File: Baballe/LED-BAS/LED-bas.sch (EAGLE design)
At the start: 15 parts, among them Q1 200mA/50V, Q2 200mA/50V, Q3 200mA/50V

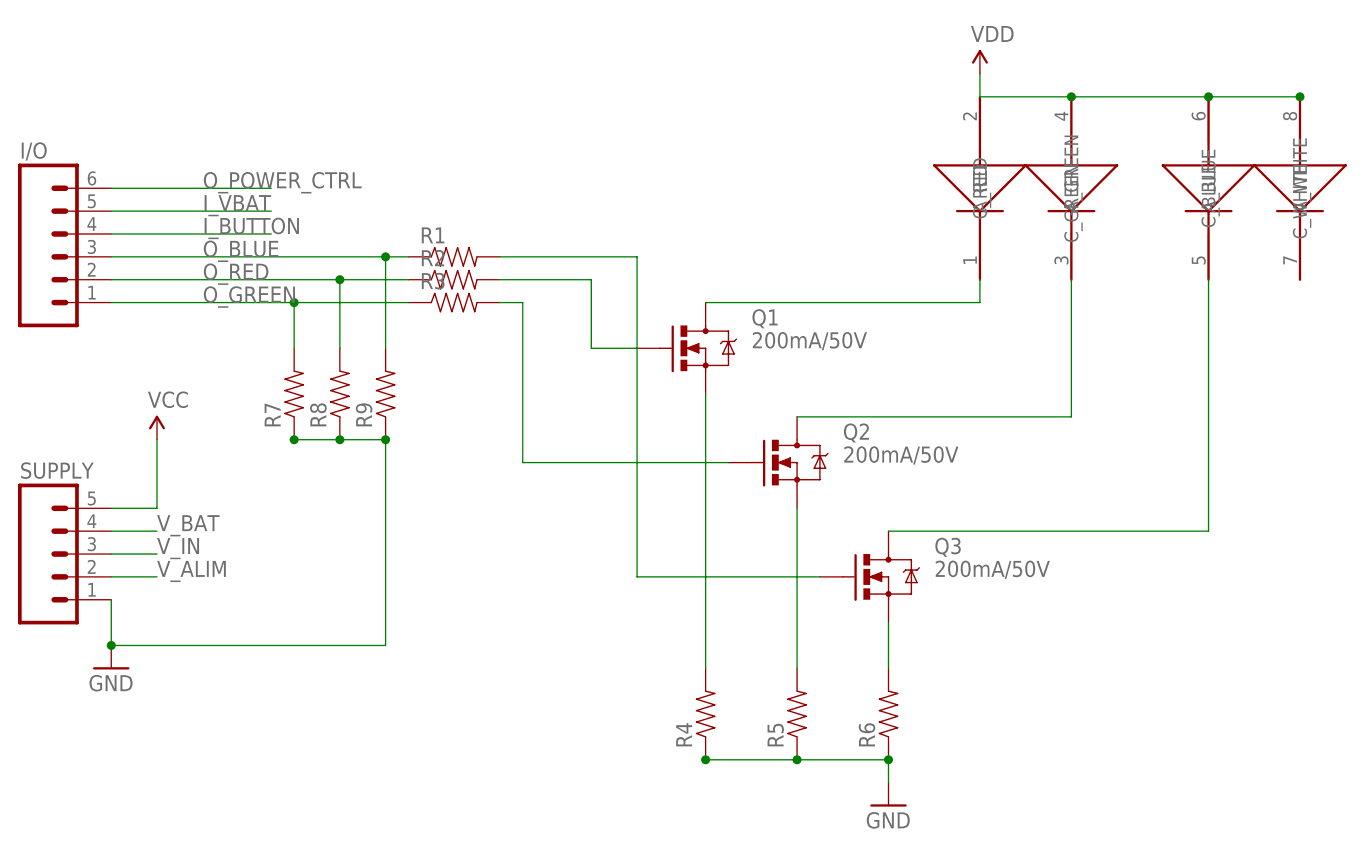
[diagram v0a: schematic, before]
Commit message: Modification sur les modules led et alimentation
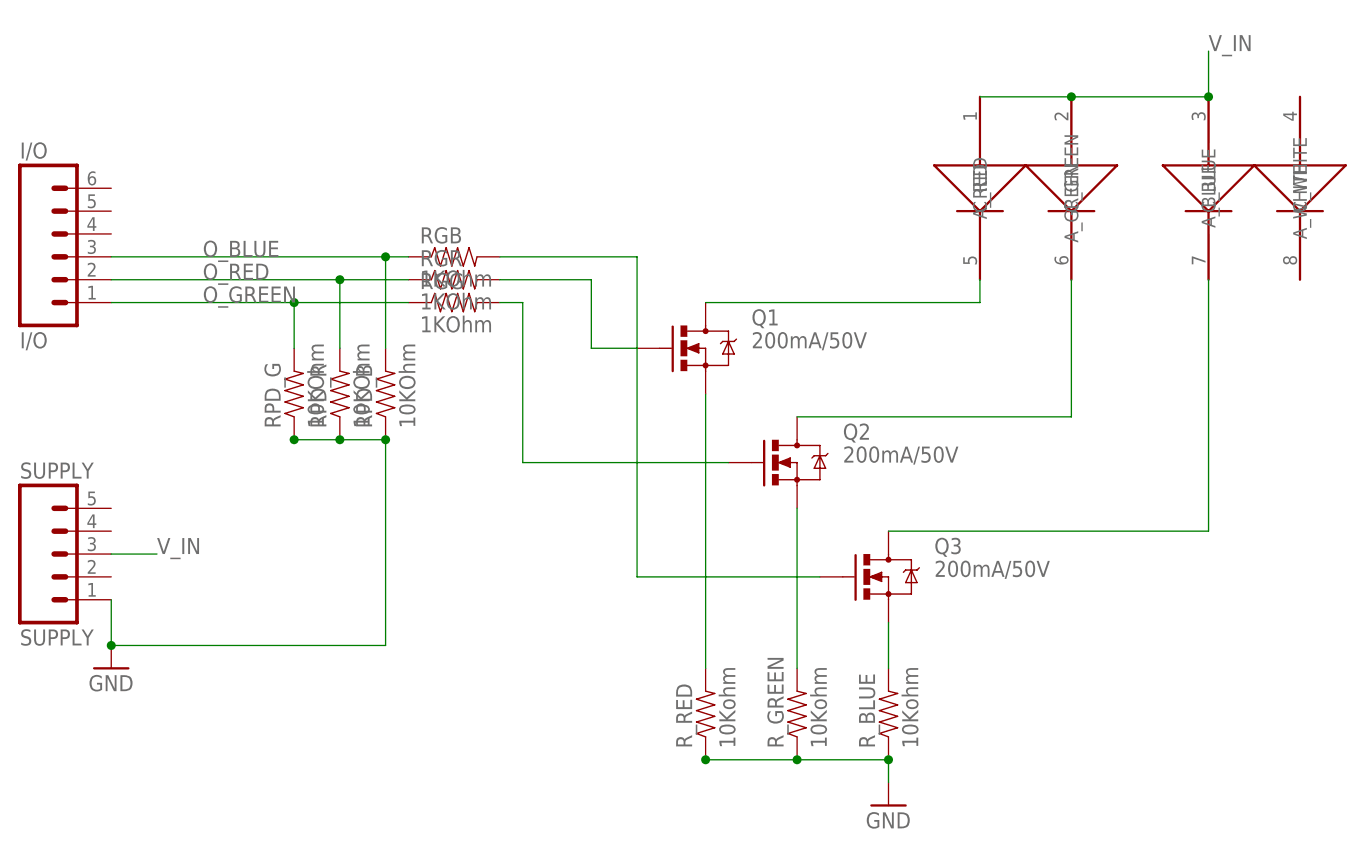
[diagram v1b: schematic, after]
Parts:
- I/O: value (none) -> I/O
- RGB, RGG, RGR: value (none) -> 1KOhm
- RPD_B, RPD_G, RPD_R: value (none) -> 10KOhm
- R_BLUE, R_GREEN, R_RED: value (none) -> 10Kohm
- SUPPLY: value (none) -> SUPPLY
- renumbered R1 to RGB, R2 to RGR, R3 to RGG, R4 to R_RED, R5 to R_GREEN, R6 to R_BLUE, R7 to RPD_G, R8 to RPD_R, R9 to RPD_B
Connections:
- removed net I_BUTTON: I/O.4
- removed net I_VBAT: I/O.5
- removed net O_POWER_CTRL: I/O.6
- removed net VCC: SUPPLY.5
- removed net V_ALIM: SUPPLY.2
- removed net V_BAT: SUPPLY.4, U$1.C_BLUE, U$1.C_GREEN, U$1.C_RED, U$1.C_WHITE
- net N$7: now also U$1.C_RED; no longer U$1.A_RED
- net N$8: now also U$1.C_GREEN; no longer U$1.A_GREEN
- net N$9: now also U$1.C_BLUE; no longer U$1.A_BLUE
- net V_IN: now also U$1.A_BLUE, U$1.A_GREEN, U$1.A_RED
